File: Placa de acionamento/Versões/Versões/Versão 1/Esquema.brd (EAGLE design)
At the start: 69.8 x 58.5 mm, 23 parts, among them Q1 IRF540, Q2 IRF540, Q3 IRF540

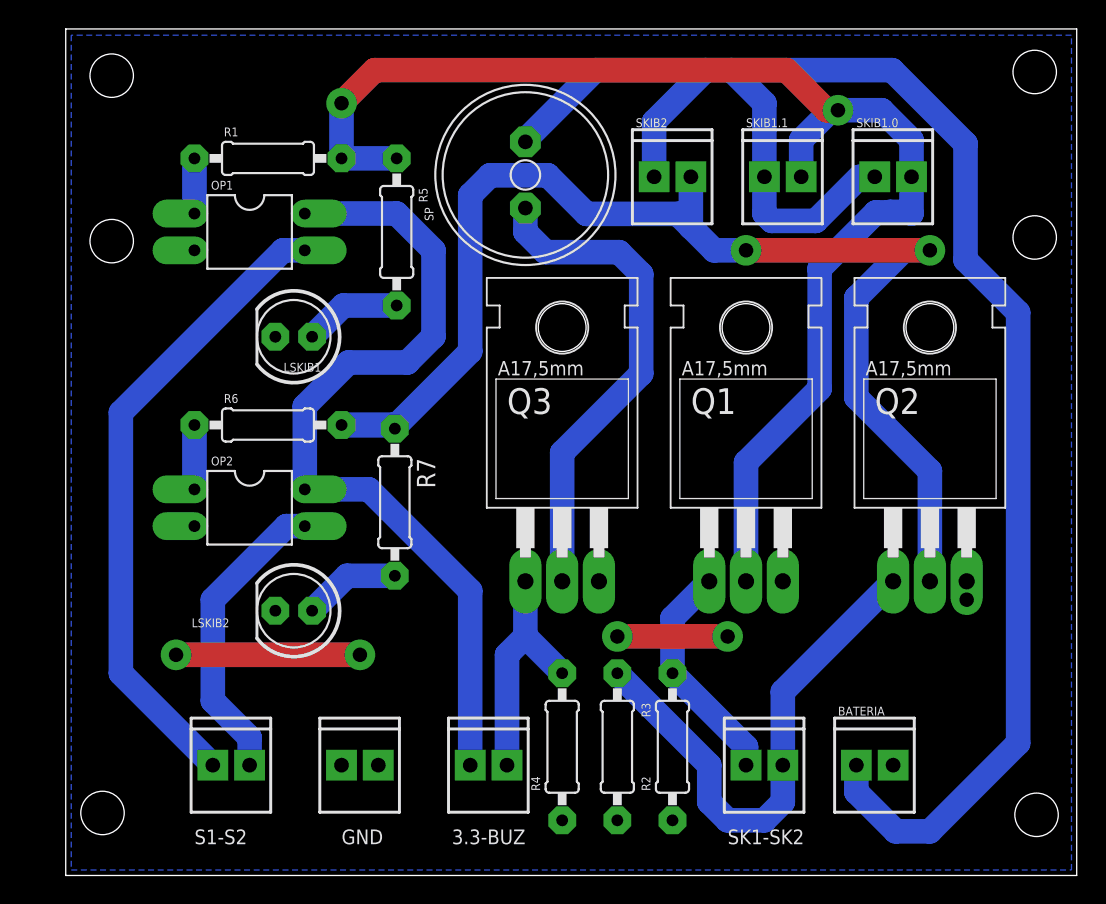
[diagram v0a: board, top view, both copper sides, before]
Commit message: CHORE: adicionando modelos 3D
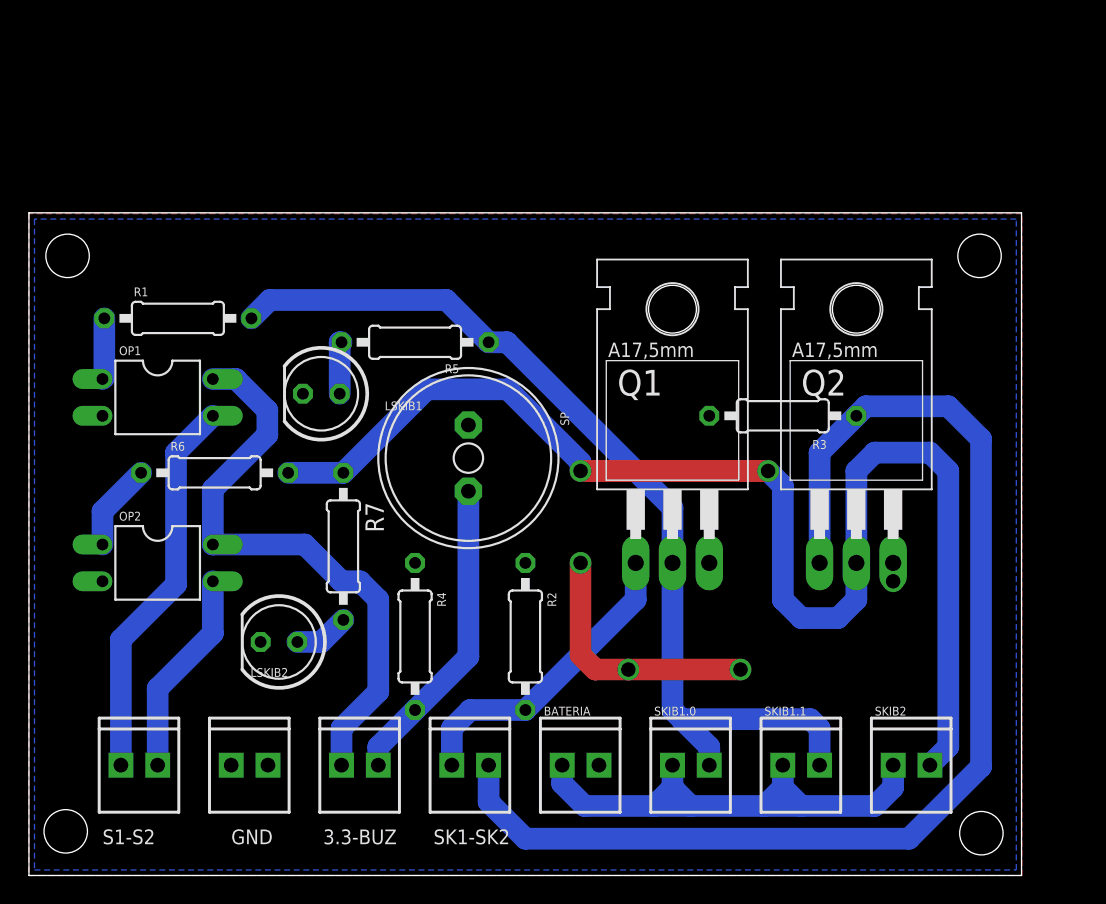
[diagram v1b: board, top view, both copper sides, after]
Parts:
- removed Q3: IRF540, transistor-fet:TO220
- moved SKIB2 43.9 mm to (57.1, 7.62)
- moved SKIB1.0 43.0 mm to (41.9, 7.62)
- moved SKIB1.1 40.7 mm to (49.5, 7.62)
- moved R3 25.6 mm to (49.5, 31.8), turned to 0 degrees
- moved BATERIA 20.3 mm to (34.3, 7.62)
- moved SK1-SK2 20.3 mm to (26.7, 7.62)
- moved SP 20.0 mm to (27.8, 28.8), turned to 270 degrees
- moved OP1 13.1 mm to (6.35, 33.0)
- moved R4 12.7 mm to (24.1, 16.5), turned to 270 degrees
- moved R2 12.7 mm to (31.8, 16.5), turned to 270 degrees
- moved R1 12.7 mm to (7.75, 38.5)
- moved 3.3-BUZ 8.89 mm to (19.1, 7.62)
- moved R5 7.73 mm to (24.1, 36.8), turned to 180 degrees
- moved GND 7.62 mm to (11.4, 7.62)
- moved OP2 7.41 mm to (6.35, 21.6)
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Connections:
- removed net N$2: Q3.2, SP.-
- net BUZZER: now also SP.+; no longer Q3.1
- net GND: now also SP.-; no longer Q3.3
- net VCC: no longer SP.+
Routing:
- net VCC: track 123.0 -> 37.1 mm
- net SKIB2: track 36.0 -> 83.3 mm
- net N$2: track 34.3 -> 0.00 mm
- net SKIB1_CONECTOR: track 92.7 -> 66.7 mm, vias 2 -> 0
- net 3.3V: track 58.9 -> 41.0 mm
- net SINAL_SKIB1: track 44.3 -> 26.8 mm
- net SINAL_SKIB2: track 20.9 -> 14.3 mm
- net SKIB1: track 15.9 -> 21.5 mm
- net BUZZER: track 16.8 -> 21.5 mm
- net N$3: track 6.74 -> 3.68 mm
- net N$1: track 6.71 -> 3.81 mm
- net GND: track 20.3 -> 17.8 mm, vias 5 -> 4
- net N$5: track 4.44 -> 6.06 mm
- net SKIB2_CONECTOR: track 91.8 -> 90.8 mm
- added copper zone on layer 1, net GND
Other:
- board size 69.8 x 58.5 mm -> 68.6 x 45.8 mm
